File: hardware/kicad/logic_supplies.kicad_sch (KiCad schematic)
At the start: 28 parts, among them U39 MCP9700AT-E/TT, U40 MCP3208-BI/SL

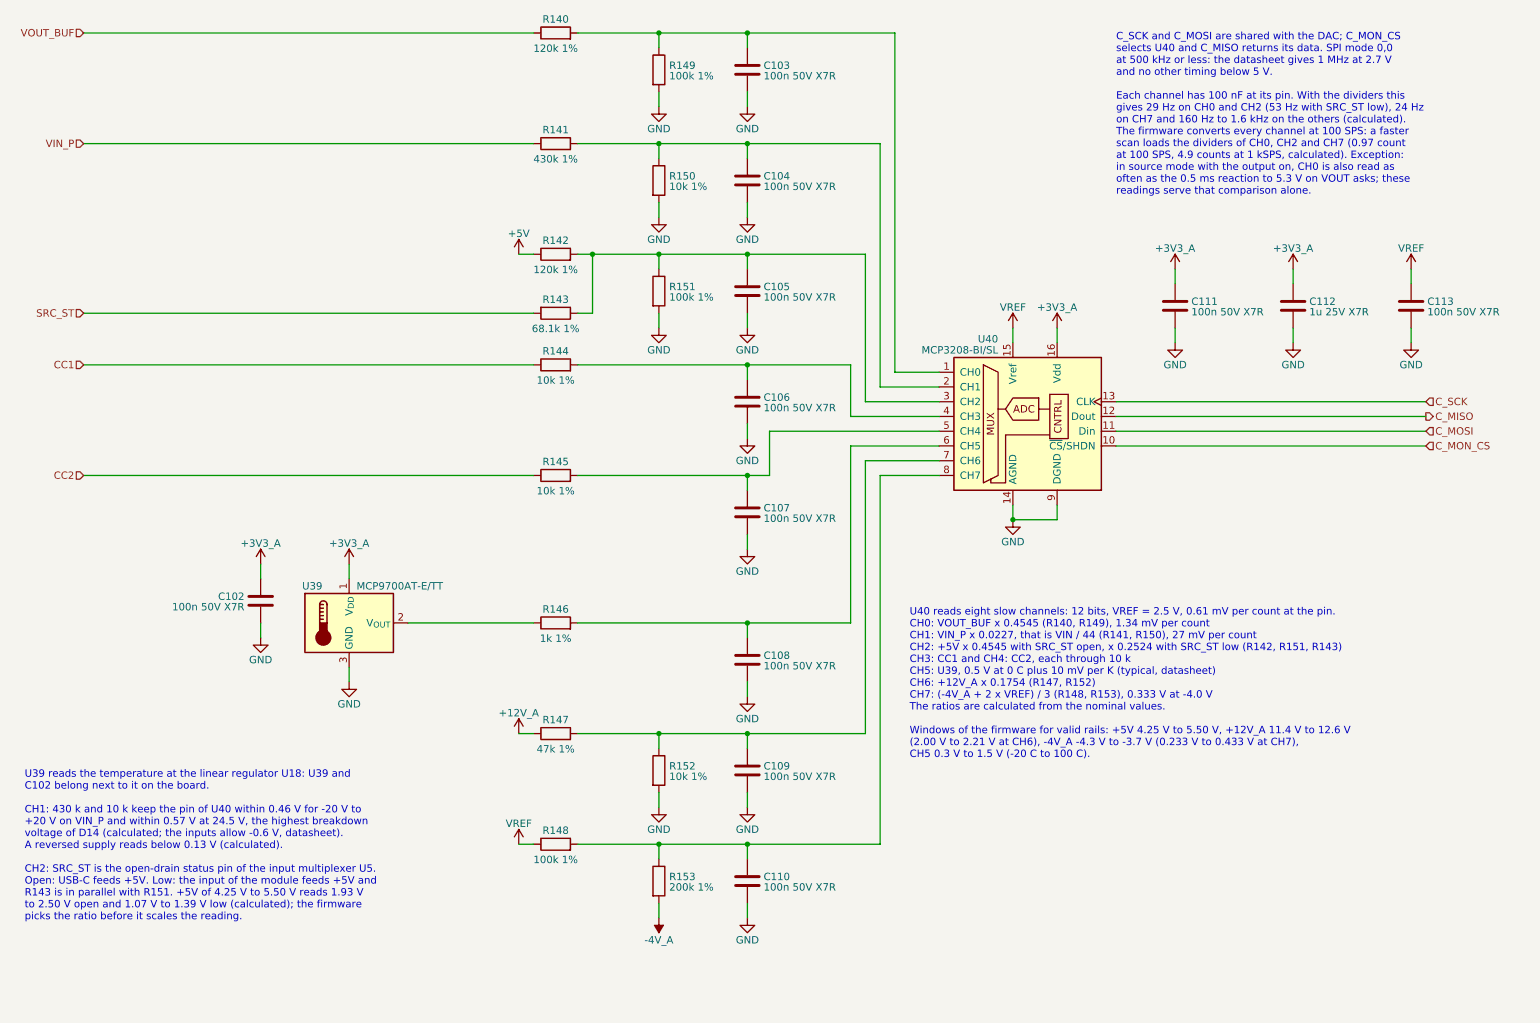
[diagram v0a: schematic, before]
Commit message: feat(hardware): draw draft A2 of the schematic
428 parts on 15 A4 pages, 14 sheets below the root sheet (D-83). Two
sheets are new: Logic Supplies, with the supervisor of the 5 V rail and
the two 3.3 V regulators, and Rail Monitor, with the comparators behind
PWR_GOOD.

The drawings follow the specification of draft A2: a current limiter
on each supply input and a priority multiplexer, a pre-regulator that
tracks the output of the linear regulator, a VIN path that withstands
-20 V to +20 V with its switch open, two diode-connected MOSFETs as
ladder clamp, thin-film and four-terminal shunts, ESD arrays at the CC
pins and at the VCC pin of the logic port. The reference designators
are numbered as KiCad numbers them (D-45), so they are not those of
draft A1.

The project library gains the symbol of the input multiplexer and two
footprints: the lever terminal block with pads of 1.9 mm x 2.3 mm and
the controller module without its antenna keep-out (D-85).

The electrical rules check reports no errors and no warnings. The
parts are candidates, and nothing is built or measured.
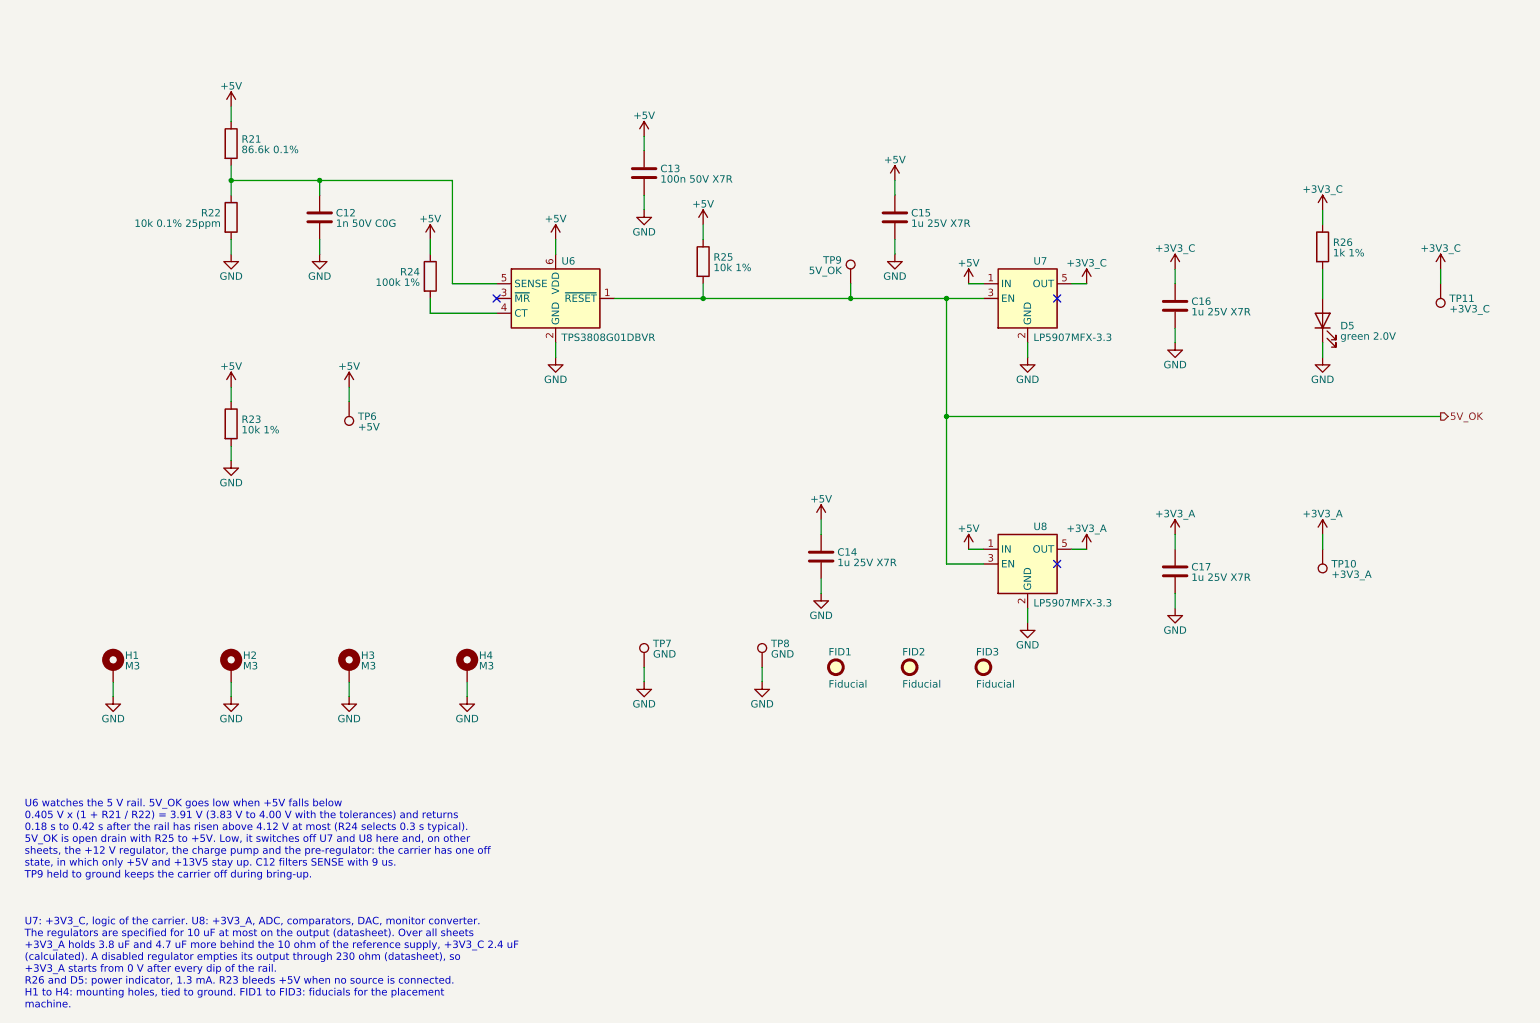
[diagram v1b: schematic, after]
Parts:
- removed C102, C103, C104, C105, C106, C107, C108, C109, C110, C111, C113: 100n 50V X7R, Capacitor_SMD:C_0603_1608Metric, symbol Device:C
- removed C112: 1u 25V X7R, Capacitor_SMD:C_0603_1608Metric, symbol Device:C
- removed R140, R142: 120k 1%, Resistor_SMD:R_0603_1608Metric, symbol Device:R
- removed R141: 430k 1%, Resistor_SMD:R_0603_1608Metric, symbol Device:R
- removed R143: 68.1k 1%, Resistor_SMD:R_0603_1608Metric, symbol Device:R
- removed R144, R145, R150, R152: 10k 1%, Resistor_SMD:R_0603_1608Metric, symbol Device:R
- removed R146: 1k 1%, Resistor_SMD:R_0603_1608Metric, symbol Device:R
- removed R147: 47k 1%, Resistor_SMD:R_0603_1608Metric, symbol Device:R
- removed R148, R149, R151: 100k 1%, Resistor_SMD:R_0603_1608Metric, symbol Device:R
- removed R153: 200k 1%, Resistor_SMD:R_0603_1608Metric, symbol Device:R
- removed U39: MCP9700AT-E/TT, Package_TO_SOT_SMD:SOT-23, symbol Sensor_Temperature:MCP9700Ax-ETT
- removed U40: MCP3208-BI/SL, Package_SO:SOIC-16_3.9x9.9mm_P1.27mm, symbol Analog_ADC:MCP3208
- added C12: 1n 50V C0G, Capacitor_SMD:C_0603_1608Metric, symbol Device:C
- added C13: 100n 50V X7R, Capacitor_SMD:C_0603_1608Metric, symbol Device:C
- added C14, C15, C16, C17: 1u 25V X7R, Capacitor_SMD:C_0603_1608Metric, symbol Device:C
- added D5: green 2.0V, LED_SMD:LED_0603_1608Metric, symbol Device:LED
- added FID1, FID2, FID3: Fiducial, Fiducial:Fiducial_1mm_Mask2mm, symbol Mechanical:Fiducial
- added H1, H2, H3, H4: M3, MountingHole:MountingHole_3.2mm_M3_Pad, symbol Mechanical:MountingHole_Pad
- added R21: 86.6k 0.1%, Resistor_SMD:R_0603_1608Metric, symbol Device:R
- added R22: 10k 0.1% 25ppm, Resistor_SMD:R_0603_1608Metric, symbol Device:R
- added R23, R25: 10k 1%, Resistor_SMD:R_0603_1608Metric, symbol Device:R
- added R24: 100k 1%, Resistor_SMD:R_0603_1608Metric, symbol Device:R
- added R26: 1k 1%, Resistor_SMD:R_0603_1608Metric, symbol Device:R
- added TP10: +3V3_A, TestPoint:TestPoint_Pad_D1.5mm, symbol Connector:TestPoint
- added TP11: +3V3_C, TestPoint:TestPoint_Pad_D1.5mm, symbol Connector:TestPoint
- added TP6: +5V, TestPoint:TestPoint_Pad_D1.5mm, symbol Connector:TestPoint
- added TP7, TP8: GND, TestPoint:TestPoint_Pad_D1.5mm, symbol Connector:TestPoint
- added TP9: 5V_OK, TestPoint:TestPoint_Pad_D1.5mm, symbol Connector:TestPoint
- added U6: TPS3808G01DBVR, Package_TO_SOT_SMD:SOT-23-6, symbol Power_Supervisor:TPS3808DBV
- added U7, U8: LP5907MFX-3.3, Package_TO_SOT_SMD:SOT-23-5, symbol Regulator_Linear:LP5907MFX-3.3
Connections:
- net +3V3_A: now also C17.1, TP10.1, U8.5 (OUT)
- net +5V: now also C13.1, C14.1, C15.1, R21.1, R23.1, R24.1, R25.1, TP6.1, U6.6 (VDD), U7.1 (IN), U8.1 (IN)
- net GND: now also C12.2, C13.2, C14.2, C15.2, C16.2, C17.2, D5.1 (K), H1.1, H2.1, H3.1, H4.1, R22.2, R23.2, TP7.1, TP8.1, U6.2 (GND), U7.2 (GND), U8.2 (GND)
- new net: R24.2, U6.4 (CT)
- new net: C12.1, R21.2, R22.1, U6.5 (SENSE)
- new net: D5.2 (A), R26.2
- new net +3V3_C: C16.1, R26.1, TP11.1, U7.5 (OUT)
- new net 5V_OK: R25.2, TP9.1, U6.1 (~{RESET}), U7.3 (EN), U8.3 (EN)
- no-connect marks 0 -> 3
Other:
- note added: "U6 watches the 5 V rail. 5V_OK goes low when +5V falls below 0.405 V x (1 + R21 / R22) = 3.91 V (3.83 V to 4.00 V with the tolerances) and returns 0.18 s to 0.42 s after the rail has risen above 4.12 V at most (R24 selects 0.3 s typical). 5V_OK is open drain with R25 to +5V. Low, it switches off U7 and U8 here and, on other sheets, the +12 V regulator, the charge pump and the pre-regulator: the c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"
- note added: "U7: +3V3_C, logic of the carrier. U8: +3V3_A, ADC, comparators, DAC, monitor converter. The regulators are specified for 10 uF at most on the output (datasheet). Over all sheets +3V3_A holds 3.8 uF and 4.7 uF more behind the 10 ohm of the reference supply, +3V3_C 2.4 uF (calculated). A disabled regulator empties its output through 230 ohm (datasheet), so +3V3_A starts from 0 V after every dip of 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"
- note removed: "C_SCK and C_MOSI are shared with the DAC; C_MON_CS selects U40 and C_MISO returns its data. SPI mode 0,0 at 500 kHz or less: the datasheet gives 1 MHz at 2.7 V and no other timing below 5 V. Each channel has 100 nF at its pin. With the dividers this gives 29 Hz on CH0 and CH2 (53 Hz with SRC_ST low), 24 Hz on CH7 and 160 Hz to 1.6 kHz on the others (calculated). The firmware converts every channe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"
- note removed: "U39 reads the temperature at the linear regulator U18: U39 and C102 belong next to it on the board. CH1: 430 k and 10 k keep the pin of U40 within 0.46 V for -20 V to +20 V on VIN_P and within 0.57 V at 24.5 V, the highest breakdown voltage of D14 (calculated; the inputs allow -0.6 V, datasheet). A reversed supply reads below 0.13 V (calculated). CH2: SRC_ST is the open-drain status pin of the in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"
- note removed: "U40 reads eight slow channels: 12 bits, VREF = 2.5 V, 0.61 mV per count at the pin. CH0: VOUT_BUF x 0.4545 (R140, R149), 1.34 mV per count CH1: VIN_P x 0.0227, that is VIN / 44 (R141, R150), 27 mV per count CH2: +5V x 0.4545 with SRC_ST open, x 0.2524 with SRC_ST low (R142, R151, R143) CH3: CC1 and CH4: CC2, each through 10 k CH5: U39, 0.5 V at 0 C plus 10 mV per K (typical, datasheet) CH6: +12V_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"
- title: Slow Monitors -> Logic Supplies and Rail Supervisor
